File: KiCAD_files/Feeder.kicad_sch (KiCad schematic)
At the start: 58 parts, among them J1 Conn_01x01, J2 Conn_01x01, J3 Conn_01x01, J4 Conn_01x01, Q1 TK13P25D,RQ, T1 PA2467NL, U2 NCP12700, U3 HMHA2801A, U4 TL431MFDT,215

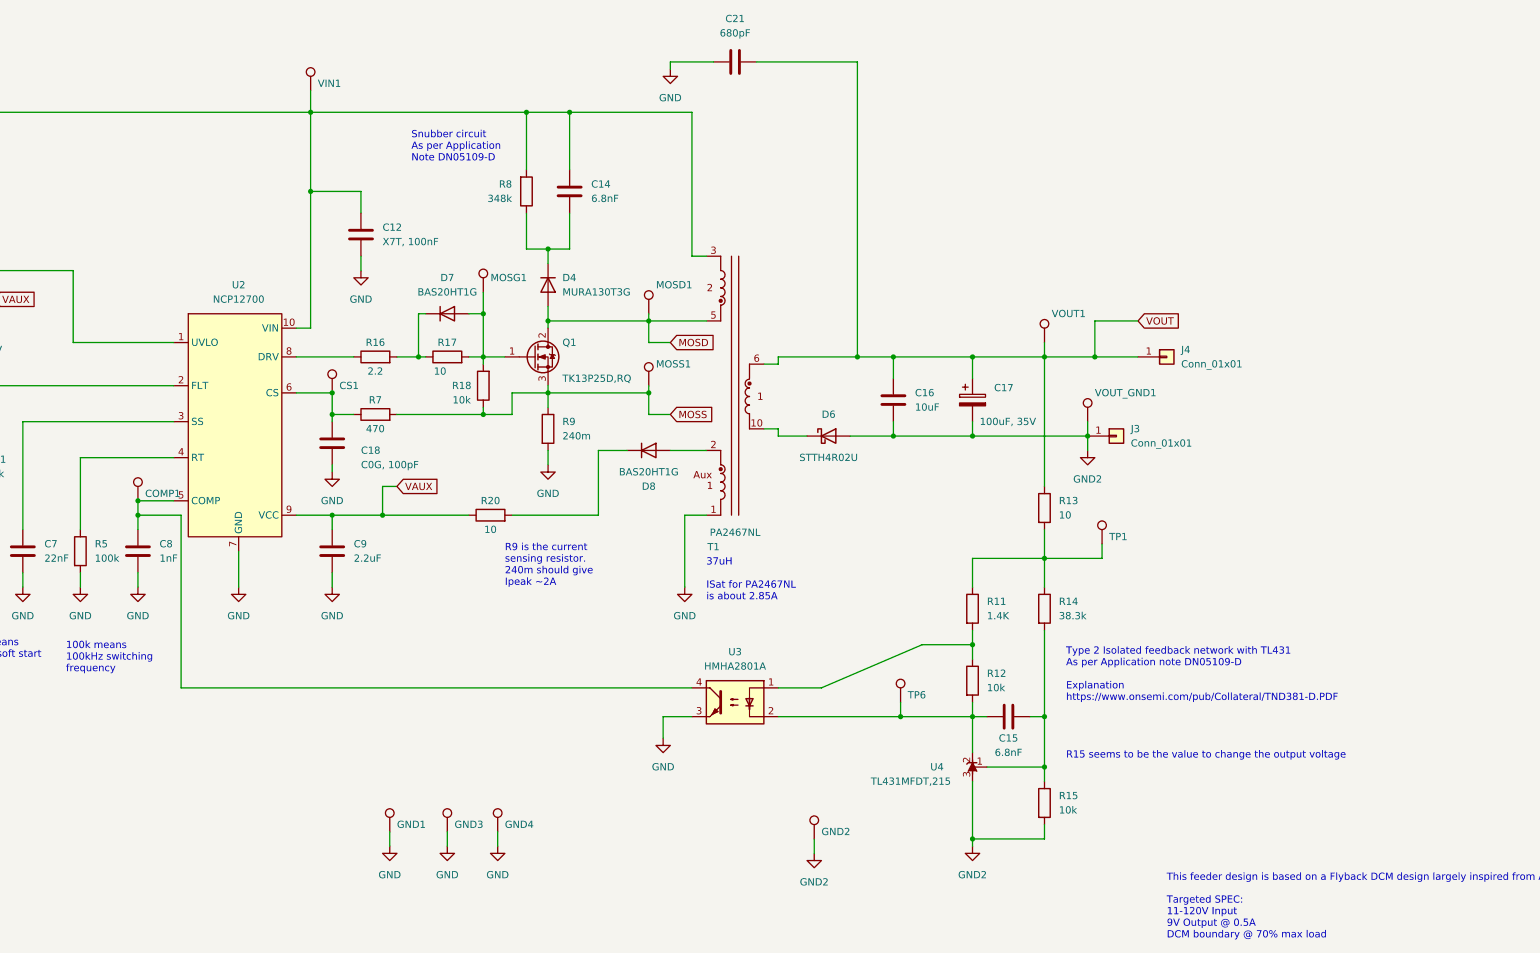
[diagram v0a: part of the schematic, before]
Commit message: Created a first routed STM32G4 module and ordered it in JLCPCB
Former-commit-id: 49804de64bb80eadc7f05c9bfca13c93680f06aa
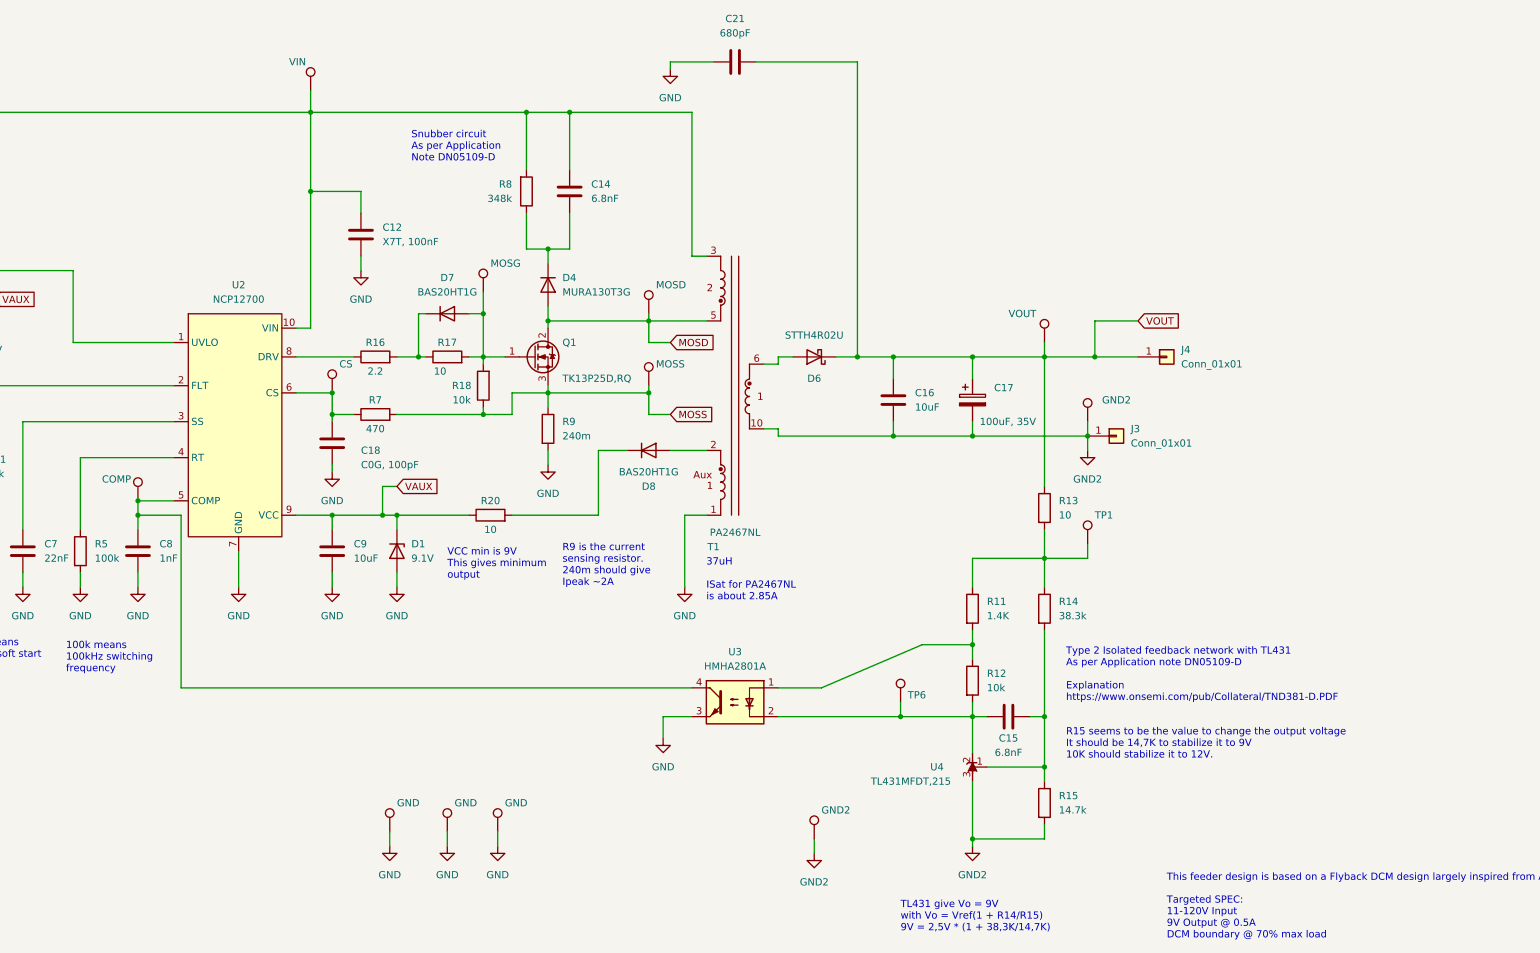
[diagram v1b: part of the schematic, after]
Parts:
- added D1: 9.1V, Diode_SMD:D_SOD-323, symbol Device:D_Zener
- C9: value 2.2uF -> 10uF; footprint Capacitor_SMD:C_0805_2012Metric -> Capacitor_SMD:C_1210_3225Metric; #manf CGA4J3X7R1H225K125AE -> UMK325C7106KM-T; Manf# CGA4J3X7R1H225K125AE -> UMK325C7106KM-T
- COMP1: value TestPoint -> COMP
- CS1: value TestPoint -> CS
- GND1, GND3, GND4: value TestPoint -> GND
- GND2, VOUT_GND1: value TestPoint -> GND2
- MOSD1: value TestPoint -> MOSD
- MOSG1: value TestPoint -> MOSG
- MOSS1: value TestPoint -> MOSS
- R15: value 10k -> 14.7k; #manf CRT0805-FZ-1002ELF -> RC0805FR-0714K7L; Manf# CRT0805-FZ-1002ELF -> RC0805FR-0714K7L
- VIN1: value TestPoint -> VIN
- VOUT1: value TestPoint -> VOUT
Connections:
- net GND: now also D1.2 (A)
- net GND2: now also T1.10; no longer D6.2 (A)
- net VAUX: now also D1.1 (K)
- net VOUT: now also D6.1 (K); no longer T1.6
- new net: D6.2 (A), T1.6
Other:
- note added: "R15 seems to be the value to change the output voltage It should be 14,7K to stabilize it to 9V 10K should stabilize it to 12V."
- note added: "TL431 give Vo = 9V with Vo = Vref(1 + R14/R15) 9V = 2,5V * (1 + 38,3K/14,7K)"
- note added: "VCC min is 9V This gives minimum output"
- note removed: "R15 seems to be the value to change the output voltage"
- moved on the sheet: D6, TP1

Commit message: [Feeder] WIP on the V2 redesign
Former-commit-id: 5bce92fb9a428cd005e74b891f189b6460f88472
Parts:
- removed COMP1: COMP, TestPoint:TestPoint_THTPad_D2.0mm_Drill1.0mm, symbol Connector:TestPoint
- removed CS1: CS, TestPoint:TestPoint_THTPad_D2.0mm_Drill1.0mm, symbol Connector:TestPoint
- removed D1: 9.1V, Diode_SMD:D_SOD-323, symbol Device:D_Zener
- removed MOSD1: MOSD, TestPoint:TestPoint_THTPad_D2.0mm_Drill1.0mm, symbol Connector:TestPoint
- removed MOSG1: MOSG, TestPoint:TestPoint_THTPad_D2.0mm_Drill1.0mm, symbol Connector:TestPoint
- removed MOSS1: MOSS, TestPoint:TestPoint_THTPad_D2.0mm_Drill1.0mm, symbol Connector:TestPoint
- removed TP1, TP6: TestPoint, TestPoint:TestPoint_THTPad_D2.0mm_Drill1.0mm, symbol Connector:TestPoint
- added C1: 1uF, Capacitor_SMD:C_0805_2012Metric, symbol Device:C
- added C10, C13, C5: 10uF, Capacitor_SMD:C_1210_3225Metric, symbol Device:C
- added C2: 100pF 1kV DNP, Capacitor_SMD:C_1206_3216Metric, symbol Device:C
- added C3: 2.2nF, Capacitor_SMD:C_1812_4532Metric, symbol Device:C
- added C4: 1nF 500V DNP, Capacitor_SMD:C_0805_2012Metric, symbol Device:C
- added D1, D2: BAS20HT1G, Diode_SMD:D_SOD-323, symbol Device:D
- added FL1: Filter_EMI_LL_1423, symbol Device:Filter_EMI_LL_1423
- added J5: Conn_01x01, Footprints:Pad_terminal, symbol Connector_Generic:Conn_01x01
- added L1: 100uH, Inductor_SMD:L_0805_2012Metric, symbol Device:L_Small
- added Q2: 60V N channel, Package_TO_SOT_SMD:SOT-23, symbol Device:Q_NMOS_GSD
- added R1, R2: 1.4K, Resistor_SMD:R_0805_2012Metric, symbol Device:R
- added R10: 10R 1W DNP, Resistor_SMD:R_2010_5025Metric, symbol Device:R
- added U1: AP1117-50, Package_TO_SOT_SMD:SOT-223-3_TabPin2, symbol Regulator_Linear:AP1117-50
- added U5: AP1117-33, Package_TO_SOT_SMD:SOT-223-3_TabPin2, symbol Regulator_Linear:AP1117-33
- C21: value 680pF -> 2.2nF; #manf 302R29W681KV3E-****-SC -> 8853622110151; Manf# 302R29W681KV3E-****-SC -> 8853622110151
- C9: value 10uF -> 1uF; footprint Capacitor_SMD:C_1210_3225Metric -> Capacitor_SMD:C_0805_2012Metric; #manf UMK325C7106KM-T -> CL21B105KBFNNNE; Manf# UMK325C7106KM-T -> CL21B105KBFNNNE
- D5: value 9.1V -> 6.2V; #manf MM3Z9V1T1G -> BZT52C6V2-TP; Manf# MM3Z9V1T1G -> BZT52C6V2-TP
- R15: value 14.7k -> 27k
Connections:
- net GND: now also C1.2, C3.1, Q2.2 (S), R1.2, R2.2
- net GND2: now also C3.2, FL1.1; no longer J3.1 (Pin_1)
- net MOSD: now also C2.1
- net MOSS: now also C2.2
- net VAUX: now also C1.1, L1.2; no longer C9.1, U2.9 (VCC)
- net VOUT: now also FL1.2, R10.2; no longer J4.1 (Pin_1)
- net at D8.1 (K): now also Q2.1 (G), R2.1; no longer R20.2
- net at D8.2 (A), T1.2: now also D2.2 (A)
- net at D6.2 (A), T1.6: now also C4.1
- new net: D1.2 (A), L1.1, Q2.3 (D)
- new net: C5.1, FL1.3, U1.3 (VI)
- new net: C10.2, C13.2, C5.2, FL1.4, J4.1 (Pin_1), U1.1 (GND), U5.1 (GND)
- new net: C4.2, R10.1
- new net: D2.1 (K), R20.2
- new net: C10.1, J3.1 (Pin_1), U1.2 (VO), U5.3 (VI)
- new net: C13.1, J5.1 (Pin_1), U5.2 (VO)
- new net VBoost: C9.1, D1.1 (K), R1.1, U2.9 (VCC)
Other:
- note added: "Passive unregulated boost permits to supply control IC from auxillary as output voltage is below 9V"
- note added: "R15 is the value to change the output voltage It should be 27K to stabilize it to 6.05V"
- note added: "TL431 give Vo = 6.05V with Vo = Vref(1 + R14/R15) 6.05V = 2,5V * (1 + 38,3K/27K)"
- note removed: "R15 seems to be the value to change the output voltage It should be 14,7K to stabilize it to 9V 10K should stabilize it to 12V."
- note removed: "TL431 give Vo = 9V with Vo = Vref(1 + R14/R15) 9V = 2,5V * (1 + 38,3K/14,7K)"
- note removed: "VCC min is 9V This gives minimum output"
- moved on the sheet: C12, C14, C15, C16, C17, C18, C19, C20, C21, C22, C6, C7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

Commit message: WIP: mooving to a single board implementation with 160x100 form factor.
Former-commit-id: e8c19d5fc5237412fb5a003591d44756dbc6e173
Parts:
- removed C10, C13, C5: 10uF, Capacitor_SMD:C_1210_3225Metric, symbol Device:C
- removed C17: 100uF, 35V, Capacitor_SMD:CP_Elec_8x10, symbol Device:C_Polarized
- removed C6: 3.3uF, 400V, Capacitor_SMD:CP_Elec_10x10, symbol Device:C_Polarized
- removed FL1: Filter_EMI_LL_1423, symbol Device:Filter_EMI_LL_1423
- removed GND2: GND2, TestPoint:TestPoint_THTPad_D2.0mm_Drill1.0mm, symbol Connector:TestPoint
- removed GND3, GND4: GND, TestPoint:TestPoint_THTPad_D2.0mm_Drill1.0mm, symbol Connector:TestPoint
- removed J3, J4, J5: Conn_01x01, Footprints:Pad_terminal, symbol Connector_Generic:Conn_01x01
- removed U1: AP1117-50, Package_TO_SOT_SMD:SOT-223-3_TabPin2, symbol Regulator_Linear:AP1117-50
- removed U5: AP1117-33, Package_TO_SOT_SMD:SOT-223-3_TabPin2, symbol Regulator_Linear:AP1117-33
- removed VIN1: VIN, TestPoint:TestPoint_THTPad_D2.0mm_Drill1.0mm, symbol Connector:TestPoint
- removed VOUT1: VOUT, TestPoint:TestPoint_THTPad_D2.0mm_Drill1.0mm, symbol Connector:TestPoint
- added J503, J504: Conn_01x01, MountingHole:MountingHole_4.3mm_M4_DIN965_Pad, symbol Connector_Generic:Conn_01x01
- J501: renamed from J1; footprint Footprints:Pad_terminal -> MountingHole:MountingHole_4.3mm_M4_DIN965_Pad
- J502: renamed from J2; footprint Footprints:Pad_terminal -> MountingHole:MountingHole_4.3mm_M4_DIN965_Pad
- renumbered C19 to C501, C20 to C502, C22 to C503, C7 to C504, C8 to C505, C18 to C506, C9 to C507, C12 to C508, C1 to C509, C14 to C510, C2 to C511, C3 to C512, C21 to C513, C4 to C514, C16 to C515, C15 to C516, D5 to D501, D1 to D502, D7 to D503, D4 to D504, D2 to D505, D8 to D506, D6 to D507, GND1 to GND501, L1 to L501, NTC1 to NTC501, Q2 to Q501, Q1 to Q502, R6 to R501, R4 to R502, R5 to R503, R1 to R504, R16 to R505, R7 to R506, R17 to R507, R18 to R508, R8 to R509, R9 to R510, R20 to R511, R2 to R512, R10 to R513, R11 to R514, R12 to R515, R13 to R516, R14 to R517, R15 to R518, T1 to T501, U2 to U501, U3 to U502, U4 to U503, VOUT_GND1 to VOUT_GND501
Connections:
- net VOUT: now also J503.1 (Pin_1)
- net GND2 renamed DGND
- net DGND: now also J504.1 (Pin_1)
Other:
- note added: "Targeted SPEC: 11-120V Input 6V Output @ 0.5A DCM boundary @ 70% max load"
- note removed: "Targeted SPEC: 11-120V Input 9V Output @ 0.5A DCM boundary @ 70% max load"

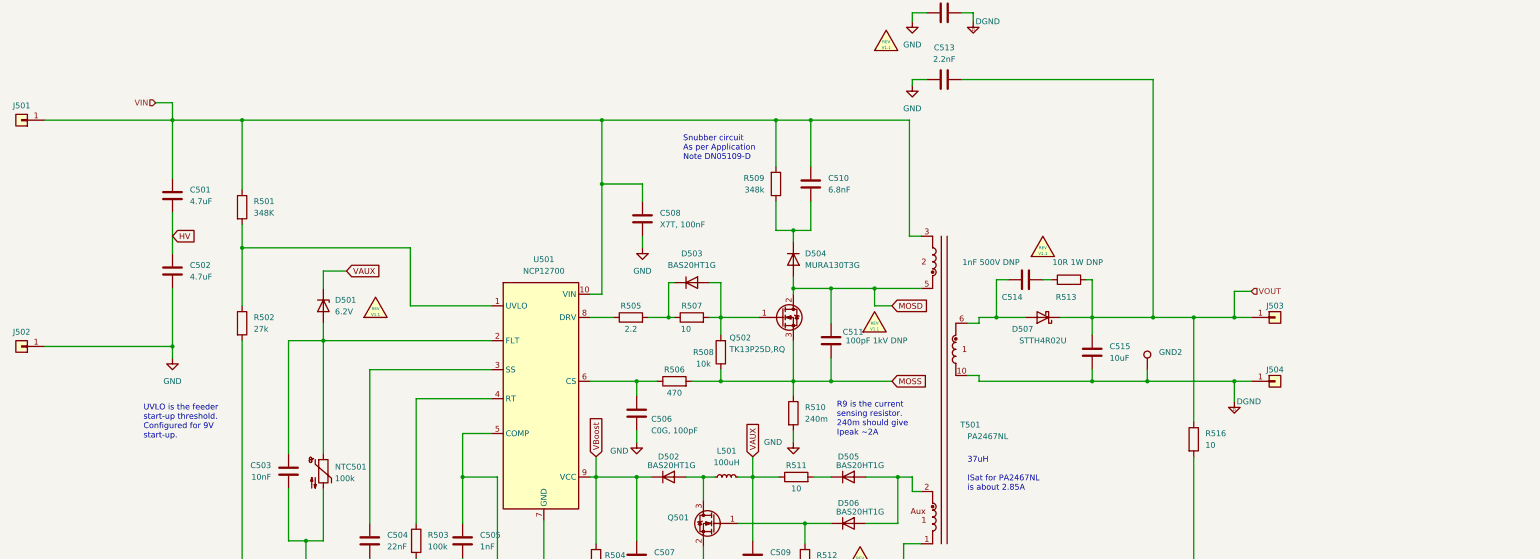
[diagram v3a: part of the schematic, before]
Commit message: WIP: integrated the feeder on the power board directly
Former-commit-id: e81265b44c994f7ae6e14a178f616f328de7a2ab
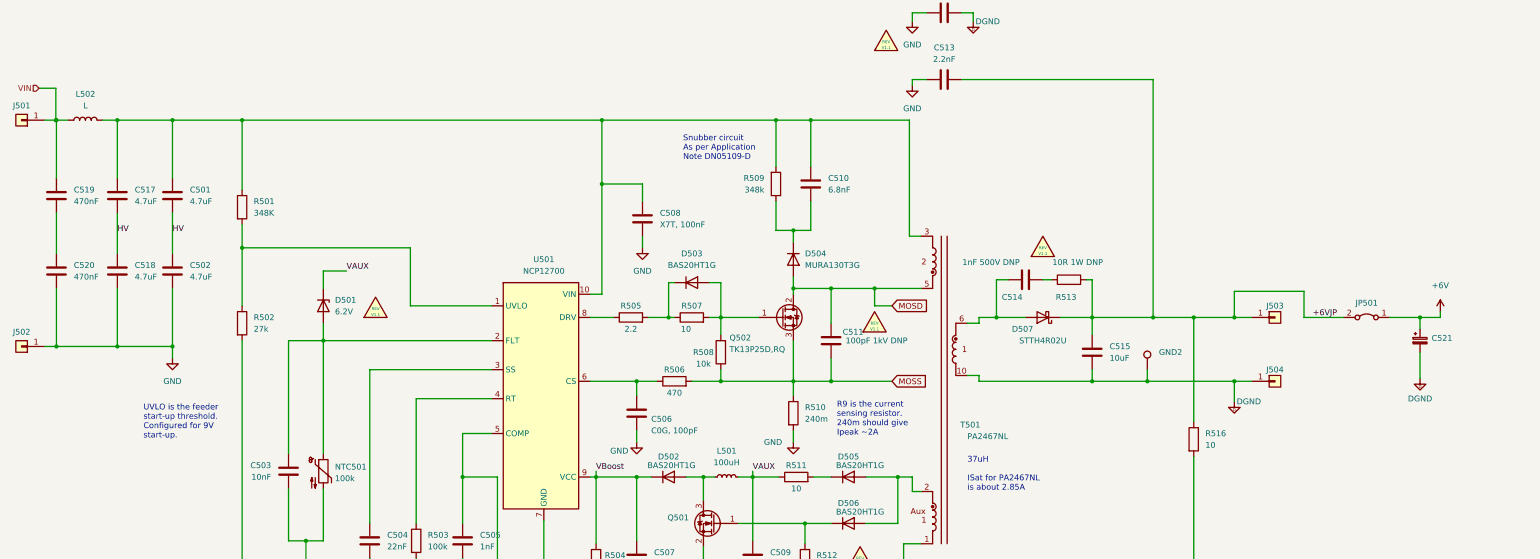
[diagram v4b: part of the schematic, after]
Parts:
- added C517, C518: 4.7uF, Capacitor_SMD:C_1210_3225Metric, symbol Device:C
- added C519, C520: 470nF, Capacitor_SMD:C_1210_3225Metric, symbol Device:C
- added C521: C_Polarized_Small, Capacitor_SMD:CP_Elec_10x10.5, symbol Device:C_Polarized_Small
- added JP501: Jumper, Connector_PinHeader_2.54mm:PinHeader_1x02_P2.54mm_Vertical, symbol Jumper:Jumper_2_Bridged
- added L502: L, symbol Device:L
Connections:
- net DGND: now also C521.2
- net GND: now also C518.2, C520.2
- net HV: now also C517.2, C518.1
- net VIN: now also C519.1, L502.1; no longer C501.1, C508.1, C510.1, R501.1, R509.2, T501.3, U501.10 (VIN)
- net VOUT renamed +6VJP
- net +6VJP: now also JP501.2 (B)
- new net: C501.1, C508.1, C510.1, C517.1, L502.2, R501.1, R509.2, T501.3, U501.10 (VIN)
- new net: C519.2, C520.1
- new net +6V: C521.1, JP501.1 (A)

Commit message: WIP : 99 percents of the nets are now routed properly
Former-commit-id: fcbb95e3f0a6512a63faba729c3990d7109d7768
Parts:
- added J505: Conn_01x03, Connector_PinHeader_2.54mm:PinHeader_1x03_P2.54mm_Vertical, symbol Connector_Generic:Conn_01x03
- C519, C520: footprint Capacitor_SMD:C_1210_3225Metric -> Capacitor_SMD:C_0805_2012Metric
- C521: value C_Polarized_Small -> 100uF; footprint Capacitor_SMD:CP_Elec_10x10.5 -> Capacitor_SMD:CP_Elec_6.3x7.7
- JP501: value Jumper -> Jumper_2_Bridged; footprint Connector_PinHeader_2.54mm:PinHeader_1x02_P2.54mm_Vertical -> Jumper:SolderJumper-2_P1.3mm_Bridged_Pad1.0x1.5mm
- L502: value L -> 10uH; footprint (none) -> Inductor_SMD:L_1210_3225Metric; Manf# (none) -> CBC3225T100M
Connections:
- net +6V: now also J505.2 (Pin_2); no longer JP501.1 (A)
- net +6VJP: now also J505.1 (Pin_1); no longer JP501.2 (B)
- net DGND: now also J505.3 (Pin_3)
- net VIN: now also JP501.1 (A); no longer C519.1, L502.1
- new net: C519.1, JP501.2 (B), L502.1
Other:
- note added: "Input 10-110V @600mA max"
- note added: "Jumper that permits to isolate the feeder if needed External supply can provide +6V from pin 2 and 3"
- note added: "Jumper that permits to isolate the feeder supply if faulty"
- note added: "Targeted SPEC: 11-110V Input 6V Output @ 0.5A DCM boundary @ 70% max load"
- note removed: "Targeted SPEC: 11-120V Input 6V Output @ 0.5A DCM boundary @ 70% max load"
- moved on the sheet: C501, C502, C503, C504, C505, C506, C507, C508, C509, C510, C511, C512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

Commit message: WIP : Mechanical drawings and fab drawings have been cleaned up
Former-commit-id: 134f220442ec2a3fea5dbd7da82e3ae2ef008ff9
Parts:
- C501, C502, C517, C518: VRating (none) -> 100V
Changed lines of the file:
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@@
+      (effects (font (size 1.27 1.27)) hide)
+    )
+    (property "VRating" "100V" (id 6) (at 60.96 80.645 0)
       (effects (font (size 1.27 1.27)) hide)
     )
@@
     )
     (property "Manf#" "DNP" (id 5) (at 48.895 80.645 0)
+      (effects (font (size 1.27 1.27)) hide)
+    )
+    (property "VRating" "100V" (id 6) (at 48.895 80.645 0)
       (effects (font (size 1.27 1.27)) hide)
     )
@@
       (effects (font (size 1.27 1.27)) hide)
     )
+    (property "VRating" "100V" (id 6) (at 48.895 64.135 0)
+      (effects (font (size 1.27 1.27)) hide)
+    )
     (pin "1")
     (pin "2")
@@
       (effects (font (size 1.27 1.27)) hide)
     )
+    (property "VRating" "100V" (id 6) (at 60.96 64.135 0)
+      (effects (font (size 1.27 1.27)) hide)
+    )

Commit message: WIP : Routed last sensors to the MCU, tweaked the courtiyards ERC almost passing
Former-commit-id: ade1cde8d39341e78235fc8e83a4a1c667a0d829
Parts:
- removed J501, J502, J503, J504: Conn_01x01, MountingHole:MountingHole_4.3mm_M4_DIN965_Pad, symbol Connector_Generic:Conn_01x01
- C501, C502, C515, C517, C518: footprint Capacitor_SMD:C_1210_3225Metric -> Footprints:C_1210_3225Metric
- C503, C504, C505, C506, C507, C508, C509, C510, C514, C516, C519, C520: footprint Capacitor_SMD:C_0805_2012Metric -> Footprints:C_0805_2012Metric
- D501, D502, D503, D505, D506: footprint Diode_SMD:D_SOD-323 -> Footprints:D_SOD-323
- NTC501, R501, R502, R503, R504, R505, R506, R507, R508, R509, R511, R512, R514, R515, R516, R517, R518: footprint Resistor_SMD:R_0805_2012Metric -> Footprints:R_0805_2012Metric
- Q501, U503: footprint Package_TO_SOT_SMD:SOT-23 -> Footprints:SOT-23_copy
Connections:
- net input: now reaches C501.1, C508.1, C510.1, C517.1, L502.2, R501.1, R509.2, T501.3, U501.10 (VIN)
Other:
- note added: "Added inductor and extra capacitors for the input filter as per application note"

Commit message: WIP : Started correcting MCU board mistakes
Former-commit-id: 0e34b6d72e10d1eac13c8cf31fc8e8f14d7f468b
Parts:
- JP501: footprint Jumper:SolderJumper-2_P1.3mm_Bridged_Pad1.0x1.5mm -> Jumper:SolderJumper-2_P1.3mm_Bridged2Bar_Pad1.0x1.5mm
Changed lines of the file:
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@@
       (effects (font (size 1.27 1.27)) hide)
     )
-    (property "Footprint" "Jumper:SolderJumper-2_P1.3mm_Bridged_Pad1.0x1.5mm" (id 2) (at 28.575 47.625 0)
+    (property "Footprint" "Jumper:SolderJumper-2_P1.3mm_Bridged2Bar_Pad1.0x1.5mm" (id 2) (at 28.575 47.625 0)
       (effects (font (size 1.27 1.27)) hide)
     )
